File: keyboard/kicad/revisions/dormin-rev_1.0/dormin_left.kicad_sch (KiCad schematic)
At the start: 116 parts, among them J1 Conn_01x06, J2 Conn_01x04, J3 Conn_01x04, Q1 AO3400A, Q2 AO3407A, SW1 SW_Push, SW10 SW_Push, SW11 SW_Push, SW12 SW_Push, SW13 SW_Push, SW14 SW_Push, SW15 SW_Push, SW16 SW_Push, SW17 SW_Push, SW18 SW_Push, SW19 SW_Push, SW2 SW_Push, SW20 SW_Push, SW3 SW_Push, SW4 SW_Push, SW5 SW_Push, SW6 SW_Push, SW7 SW_Push, SW8 SW_Push, SW9 SW_Push, U3 XIAO-nRF52840-Plus-SMD, U4 TPD2E2U06DCK

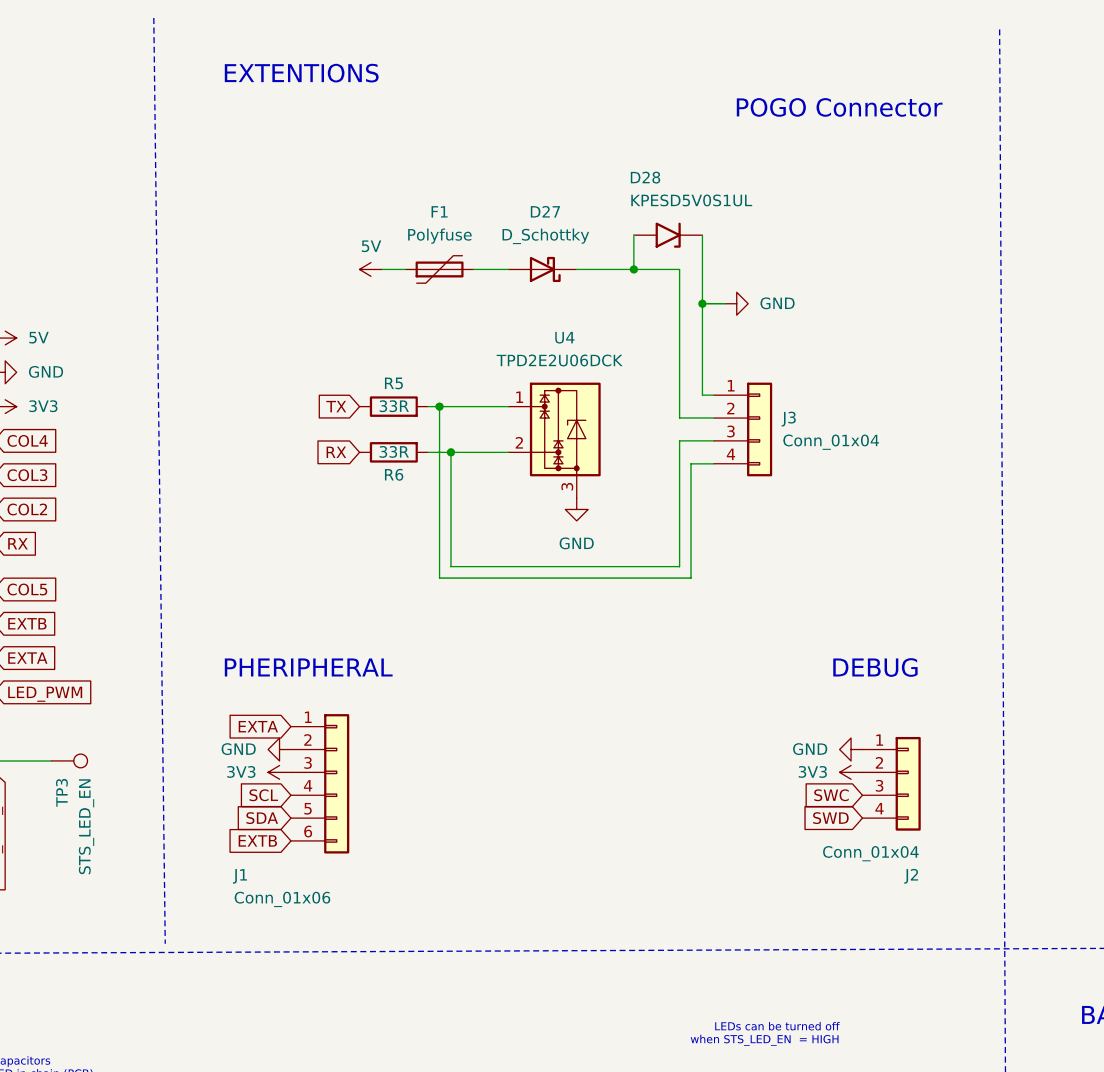
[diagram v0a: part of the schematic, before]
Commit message: feat: updated pogo-pin schematics
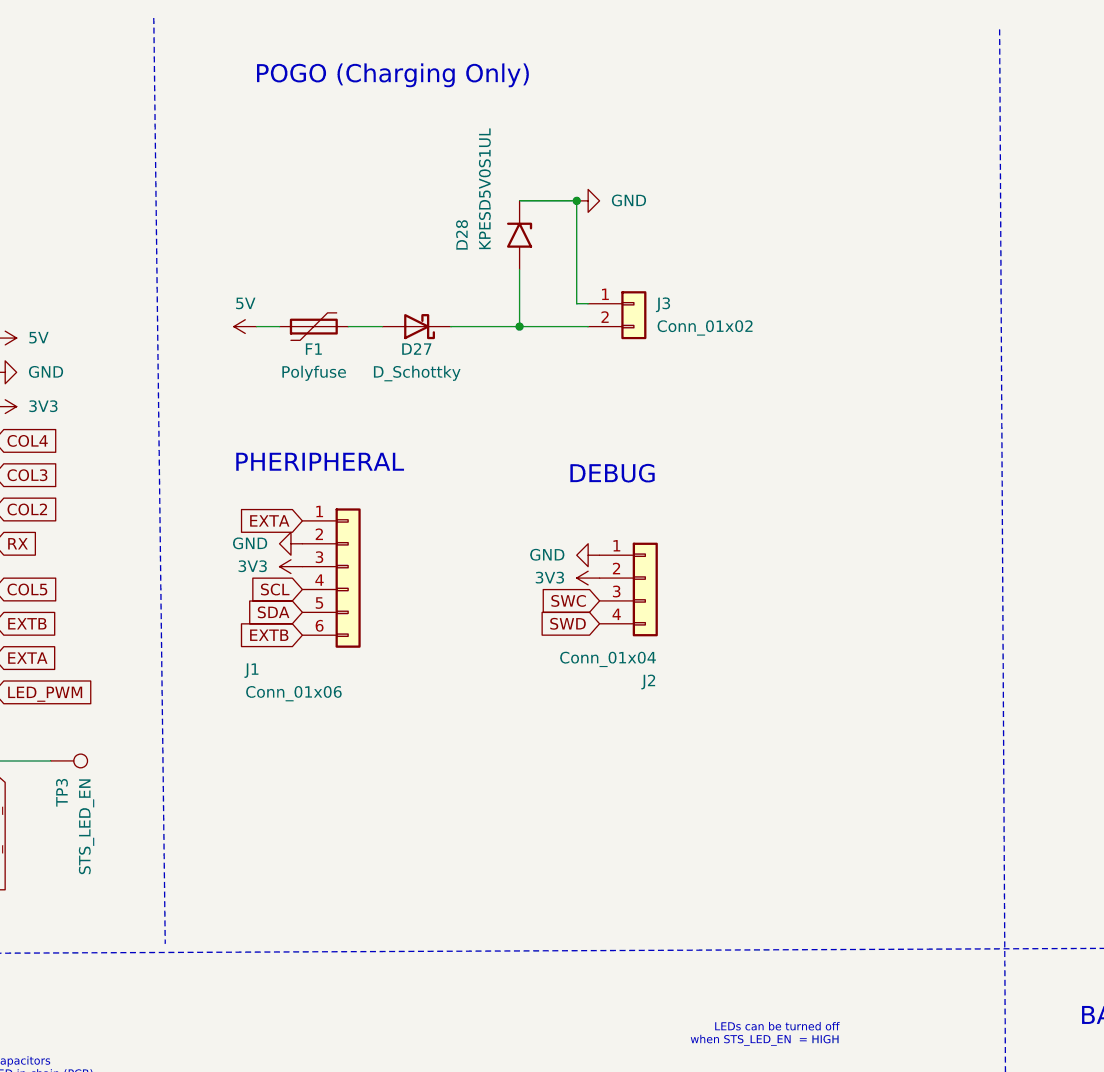
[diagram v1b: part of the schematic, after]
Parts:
- removed J3: Conn_01x04, willkeebs_misc:SMD_Conn_1x04_P2.54mm_Vertical, symbol Connector_Generic:Conn_01x04
- removed R5, R6: 33R, Resistor_SMD:R_0603_1608Metric, symbol Device:R
- removed U4: TPD2E2U06DCK, Package_TO_SOT_SMD:SOT-323_SC-70, symbol Power_Protection:TPD2E2U06DCK
- added J3: Conn_01x02, symbol Connector_Generic:Conn_01x02
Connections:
- net GND: now also J3.1 (Pin_1)
- net at D27.1 (K), D28.2 (A2): now also J3.2 (Pin_2)
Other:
- note added: "POGO (Charging Only)"
- note removed: "EXTENTIONS"
- note removed: "POGO Connector"
- moved on the sheet: D27, D28, F1, J1, J2

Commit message: feat: added initial components to the right places
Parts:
- J3: footprint (none) -> willkeebs_misc:SMD_Conn_1x02_P2.54mm_Vertical
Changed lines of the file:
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@@
 			)
 		)
-		(property "Footprint" ""
+		(property "Footprint" "willkeebs_misc:SMD_Conn_1x02_P2.54mm_Vertical"
 			(at 135.89 44.45 0)
 			(hide yes)

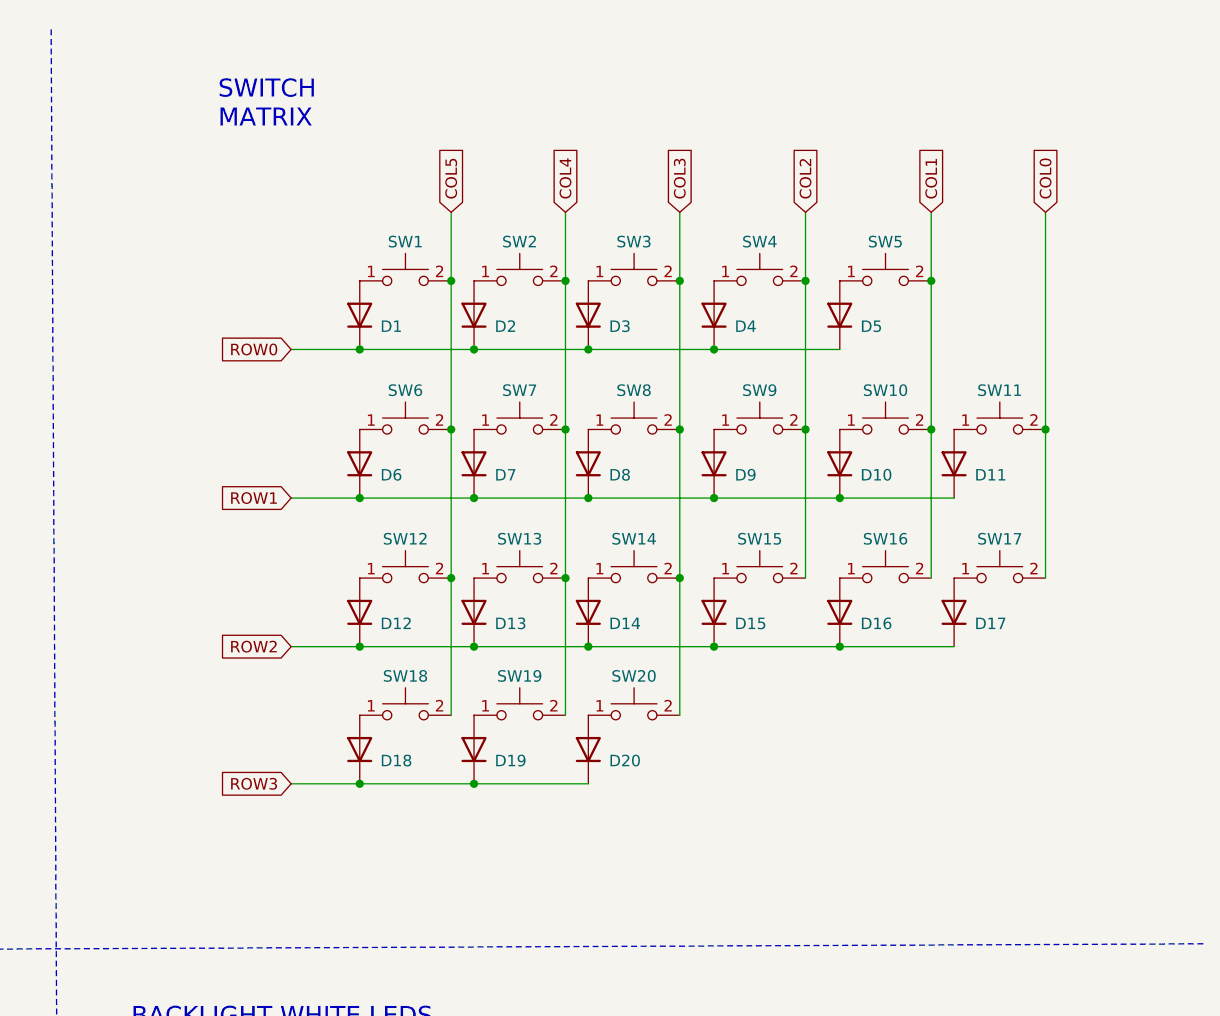
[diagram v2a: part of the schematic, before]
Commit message: feat: adjust schematics for the switches logic order
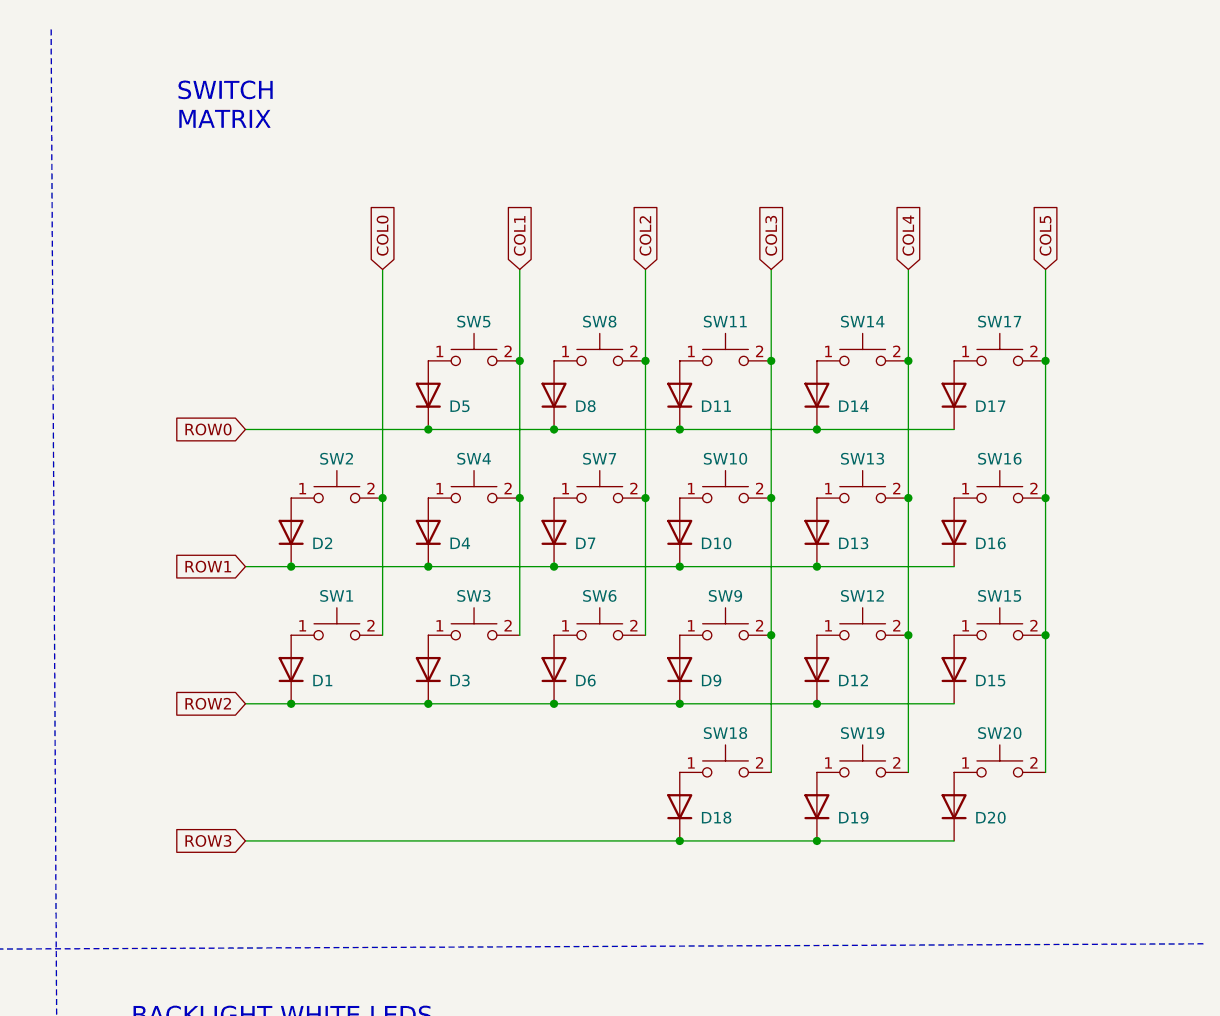
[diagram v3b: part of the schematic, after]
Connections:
- net COL0: now also SW1.2, SW2.2; no longer SW11.2, SW17.2
- net COL1: now also SW3.2, SW4.2; no longer SW10.2, SW16.2
- net COL2: now also SW6.2, SW7.2, SW8.2; no longer SW15.2, SW4.2, SW9.2
- net COL3: now also SW10.2, SW11.2, SW18.2, SW9.2; no longer SW14.2, SW20.2, SW3.2, SW8.2
- net COL4: now also SW12.2, SW14.2; no longer SW2.2, SW7.2
- net COL5: now also SW15.2, SW16.2, SW17.2, SW20.2; no longer SW1.2, SW12.2, SW18.2, SW6.2
- net ROW0: now also D11.1 (K), D14.1 (K), D17.1 (K), D8.1 (K); no longer D1.1 (K), D2.1 (K), D3.1 (K), D4.1 (K)
- net ROW1: now also D13.1 (K), D16.1 (K), D2.1 (K), D4.1 (K); no longer D11.1 (K), D6.1 (K), D8.1 (K), D9.1 (K)
- net ROW2: now also D1.1 (K), D3.1 (K), D6.1 (K), D9.1 (K); no longer D13.1 (K), D14.1 (K), D16.1 (K), D17.1 (K)
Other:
- moved on the sheet: D1, D10, D11, D12, D13, D14, D15, D16, D17, D18, D19, D2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

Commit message: feat: added routing to the left pcb
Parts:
- added MH5, MH6: MountingHole_2.2mm_M2, MountingHole:MountingHole_2.2mm_M2, symbol Mechanical:MountingHole
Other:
- moved on the sheet: MH1, MH2, MH3, MH4
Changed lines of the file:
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@@
 	(text "MOUNTING HOLES"
 		(exclude_from_sim no)
-		(at 137.668 175.514 0)
+		(at 138.43 173.99 0)
 		(effects
 			(font
@@
 	(symbol
 		(lib_id "Mechanical:MountingHole")
-		(at 139.7 182.88 0)
+		(at 139.7 179.07 0)
 		(unit 1)
 		(body_style 1)
@@
 		(dnp no)
 		(property "Reference" "MH1"
-			(at 143.256 181.6099 0)
+			(at 143.256 177.7999 0)
 			(show_name no)
 			(do_not_autoplace no)
@@
 		)
 		(property "Value" "MountingHole_2.2mm_M2"
-			(at 143.256 184.1499 0)
+			(at 143.256 180.3399 0)
 			(show_name no)
 			(do_not_autoplace no)
@@
 		)
 		(property "Footprint" "MountingHole:MountingHole_2.2mm_M2"
-			(at 139.7 182.88 0)
+			(at 139.7 179.07 0)
 			(hide yes)
 			(show_name no)
@@
 		)
 		(property "Datasheet" ""
-			(at 139.7 182.88 0)
+			(at 139.7 179.07 0)
 			(hide yes)
 			(show_name no)
@@
 		)
 		(property "Description" ""
-			(at 139.7 182.88 0)
+			(at 139.7 179.07 0)
 			(hide yes)
 			(show_name no)
@@
 	)
 	(symbol
+		(lib_id "Mechanical:MountingHole")
+		(at 139.7 199.39 0)
+		(unit 1)
+		(body_style 1)
+		(exclude_from_sim no)
+		(in_bom yes)
+		(on_board yes)
+		(in_pos_files yes)
+		(dnp no)
+		(property "Reference" "MH5"
+			(at 143.256 198.1199 0)
+			(show_name no)
+			(do_not_autoplace no)
+			(effects
+				(font
+					(size 1.27 1.27)
+				)
+				(justify left)
+			)
+		)
+		(property "Value" "MountingHole_2.2mm_M2"
+			(at 143.256 200.6599 0)
+			(show_name no)
+			(do_not_autoplace no)
+			(effects
+				(font
+					(size 1.27 1.27)
+				)
+				(justify left)
+			)
+		)
+		(property "Footprint" "MountingHole:MountingHole_2.2mm_M2"
+			(at 139.7 199.39 0)
+			(hide yes)
+			(show_name no)
+			(do_not_autoplace no)
+			(effects
+				(font
+					(size 1.27 1.27)
+				)
+			)
+		)
+		(property "Datasheet" ""
+			(at 139.7 199.39 0)
+			(hide yes)
+			(show_name no)
+			(do_not_autoplace no)
+			(effects
+				(font
+					(size 1.27 1.27)
+				)
+			)
+		)
+		(property "Description" ""
+			(at 139.7 199.39 0)
+			(hide yes)
+			(show_name no)
+			(do_not_autoplace no)
+			(effects
+				(font
+					(size 1.27 1.27)
+				)
+			)
+		)
+		(instances
+			(project "dormin"
+				(path "/603afaa0-4142-4673-b835-76ba767ab9eb/61f422a6-c5c1-4994-83bd-f5d919e1e268"
+					(reference "MH5")
+					(unit 1)
+				)
+			)
+		)
+	)
+	(symbol
 		(lib_id "Connector_Generic:Conn_01x02")
 		(at 135.89 44.45 0)
@@
 	(symbol
 		(lib_id "Mechanical:MountingHole")
-		(at 139.7 198.12 0)
+		(at 139.7 194.31 0)
 		(unit 1)
 		(body_style 1)
@@
 		(dnp no)
 		(property "Reference" "MH4"
-			(at 143.256 196.8499 0)
+			(at 143.256 193.0399 0)
 			(show_name no)
 			(do_not_autoplace no)
@@
 		)
 		(property "Value" "MountingHole_2.2mm_M2"
-			(at 143.256 199.3899 0)
+			(at 143.256 195.5799 0)
 			(show_name no)
 			(do_not_autoplace no)
@@
 		)
 		(property "Footprint" "MountingHole:MountingHole_2.2mm_M2"
-			(at 139.7 198.12 0)
+			(at 139.7 194.31 0)
 			(hide yes)
 			(show_name no)
@@
 		)
 		(property "Datasheet" ""
-			(at 139.7 198.12 0)
+			(at 139.7 194.31 0)
 			(hide yes)
 			(show_name no)
@@
 		)
 		(property "Description" ""
-			(at 139.7 198.12 0)
+			(at 139.7 194.31 0)
 			(hide yes)
 			(show_name no)
@@
 	)
 	(symbol
+		(lib_id "Mechanical:MountingHole")
+		(at 139.7 204.47 0)
+		(unit 1)
+		(body_style 1)
+		(exclude_from_sim no)
+		(in_bom yes)
+		(on_board yes)
+		(in_pos_files yes)
+		(dnp no)
+		(property "Reference" "MH6"
+			(at 143.256 203.1999 0)
+			(show_name no)
+			(do_not_autoplace no)
+			(effects
+				(font
+					(size 1.27 1.27)
+				)
+				(justify left)
+			)
+		)
+		(property "Value" "MountingHole_2.2mm_M2"
+			(at 143.256 205.7399 0)
+			(show_name no)
+			(do_not_autoplace no)
+			(effects
+				(font
+					(size 1.27 1.27)
+				)
+				(justify left)
+			)
+		)
+		(property "Footprint" "MountingHole:MountingHole_2.2mm_M2"
+			(at 139.7 204.47 0)
+			(hide yes)
+			(show_name no)
+			(do_not_autoplace no)
+			(effects
+				(font
+					(size 1.27 1.27)
+				)
+			)
+		)
+		(property "Datasheet" ""
+			(at 139.7 204.47 0)
+			(hide yes)
+			(show_name no)
+			(do_not_autoplace no)
+			(effects
+				(font
+					(size 1.27 1.27)
+				)
+			)
+		)
+		(property "Description" ""
+			(at 139.7 204.47 0)
+			(hide yes)
+			(show_name no)
+			(do_not_autoplace no)
+			(effects
+				(font
+					(size 1.27 1.27)
+				)
+			)
+		)
+		(instances
+			(project "dormin"
+				(path "/603afaa0-4142-4673-b835-76ba767ab9eb/61f422a6-c5c1-4994-83bd-f5d919e1e268"
+					(reference "MH6")
+					(unit 1)
+				)
+			)
+		)
+	)
+	(symbol
 		(lib_id "Diode:1N4148W")
 		(at 232.41 69.85 90)
@@
 	(symbol
 		(lib_id "Mechanical:MountingHole")
-		(at 139.7 187.96 0)
+		(at 139.7 184.15 0)
 		(unit 1)
 		(body_style 1)
@@
 		(dnp no)
 		(property "Reference" "MH2"
-			(at 143.256 186.6899 0)
+			(at 143.256 182.8799 0)
 			(show_name no)
 			(do_not_autoplace no)
@@
 		)
 		(property "Value" "MountingHole_2.2mm_M2"
-			(at 143.256 189.2299 0)
+			(at 143.256 185.4199 0)
 			(show_name no)
 			(do_not_autoplace no)
@@
 		)
 		(property "Footprint" "MountingHole:MountingHole_2.2mm_M2"
-			(at 139.7 187.96 0)
+			(at 139.7 184.15 0)
 			(hide yes)
 			(show_name no)
@@
 		)
 		(property "Datasheet" ""
-			(at 139.7 187.96 0)
+			(at 139.7 184.15 0)
 			(hide yes)
 			(show_name no)
@@
 		)
 		(property "Description" ""
-			(at 139.7 187.96 0)
+			(at 139.7 184.15 0)
 			(hide yes)
 			(show_name no)
@@
 	(symbol
 		(lib_id "Mechanical:MountingHole")
-		(at 139.7 193.04 0)
+		(at 139.7 189.23 0)
 		(unit 1)
 		(body_style 1)
@@
 		(dnp no)
 		(property "Reference" "MH3"
-			(at 143.256 191.7699 0)
+			(at 143.256 187.9599 0)
 			(show_name no)
 			(do_not_autoplace no)
@@
 		)
 		(property "Value" "MountingHole_2.2mm_M2"
-			(at 143.256 194.3099 0)
+			(at 143.256 190.4999 0)
 			(show_name no)
 			(do_not_autoplace no)
@@
 		)
 		(property "Footprint" "MountingHole:MountingHole_2.2mm_M2"
-			(at 139.7 193.04 0)
+			(at 139.7 189.23 0)
 			(hide yes)
 			(show_name no)
@@
 		)
 		(property "Datasheet" ""
-			(at 139.7 193.04 0)
+			(at 139.7 189.23 0)
 			(hide yes)
 			(show_name no)
@@
 		)
 		(property "Description" ""
-			(at 139.7 193.04 0)
+			(at 139.7 189.23 0)
 			(hide yes)
 			(show_name no)

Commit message: feat: added new pcb design
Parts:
- J3: footprint willkeebs_misc:SMD_Conn_1x02_P2.54mm_Vertical -> willkeebs_components:Pogo1x2-Right-Angle
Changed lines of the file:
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@@
 			)
 		)
-		(property "Footprint" "willkeebs_misc:SMD_Conn_1x02_P2.54mm_Vertical"
+		(property "Footprint" "willkeebs_components:Pogo1x2-Right-Angle"
 			(at 135.89 44.45 0)
 			(hide yes)

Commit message: feat: remove unused components for v1
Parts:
- removed D27: D_Schottky, Diode_SMD:D_SOD-523, symbol Device:D_Schottky
- removed D28: KPESD5V0S1UL, Diode_SMD:D_SOD-882, symbol Diode:SMF5V0A
- removed F1: Polyfuse, Fuse:Fuse_1206_3216Metric, symbol Device:Polyfuse
- removed J1: Conn_01x06, willkeebs_misc:SMD_Conn_1x06_P2.54mm_Vertical, symbol Connector_Generic:Conn_01x06
- removed J3: Conn_01x02, willkeebs_components:Pogo1x2-Right-Angle, symbol Connector_Generic:Conn_01x02
- removed MH1, MH2, MH3, MH4, MH5, MH6: MountingHole_2.2mm_M2, MountingHole:MountingHole_2.2mm_M2, symbol Mechanical:MountingHole
- removed U3: XIAO-nRF52840-Plus-SMD, Seeed_Studio_XIAO_Series:XIAO-nRF52840-Plus-SMD, symbol Seeed_Studio_XIAO_Series:XIAO-nRF52840_Plus_SMD
- added U1: Seeeduino Xiao nRF52840, Seeed_Studio_XIAO_Series:XIAO-nRF52840-SMD, symbol PCM_marbastlib-promicroish:Seeeduino_Xiao_nRF52840
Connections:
- net 3V3: now also U1.10 (3V3)
- net COL0: now also U1.5 (P0.04_SDA)
- net COL1: now also U1.6 (P0.05_SCL)
- net COL2: now also U1.7 (P1.11_TX)
- net COL3: now also U1.14 (P1.12_RX)
- net COL4: now also U1.13 (P1.13_SCK)
- net COL5: now also U1.12 (P1.14_MISO)
- net GND: now also U1.15 (BAT-), U1.22 (GND), U1.9 (GND)
- net LED_PWM: now also U1.11 (P1.15_MOSI)
- net RESET: now also U1.21 (RST)
- net ROW0: now also U1.1 (P0.02)
- net ROW1: now also U1.2 (P0.03)
- net ROW2: now also U1.3 (P0.28)
- net ROW3: now also U1.4 (P0.29)
- net STS_LED_DATA: now also U1.17 (P0.09)
- net STS_LED_EN: now also U1.18 (P0.10)
- net SWC: now also U1.20 (CLK)
- net SWD: now also U1.19 (DIO)
- net VBAT: now also U1.16 (BAT+)
- no-connect marks 2 -> 3
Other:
- note added: "MCU"
- note removed: "MOUNTING HOLES"
- note removed: "PHERIPHERAL"
- note removed: "POGO (Charging Only)"
- moved on the sheet: J2
